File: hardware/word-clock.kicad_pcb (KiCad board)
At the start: 2 copper layers, 177.8 x 177.8 mm, 54 parts, among them SW1 Minute, SW2 Audio, SW3 Hour, U1 ESP32 CP2102, U2 74HC245

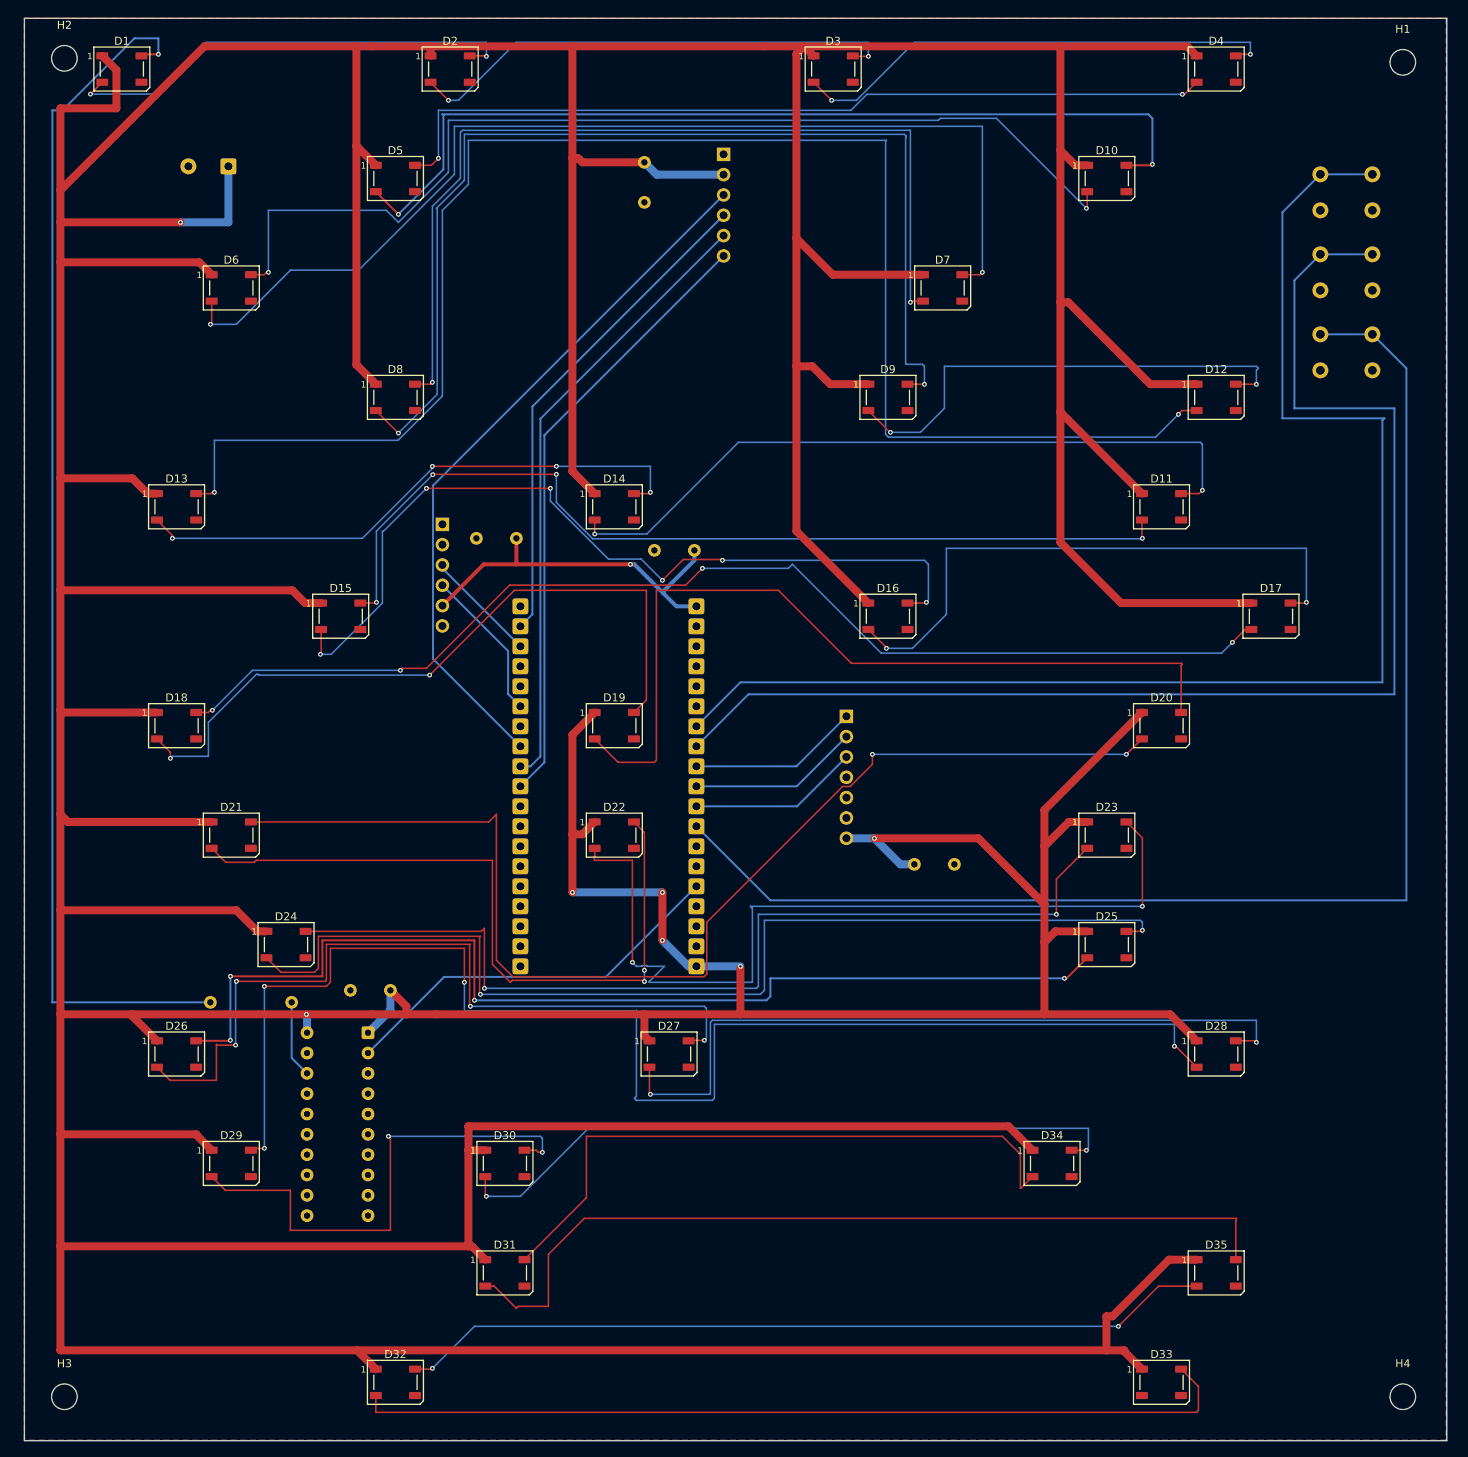
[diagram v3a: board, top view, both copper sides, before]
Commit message: feat(hardware): commit as-fabricated 63-LED board
The 63-LED board ordered from JLCPCB 2026-06-07 lived only in the working
tree and an untracked fab zip; the last hardware commit was the
superseded 35-LED April design. Commit the canonical KiCad source, the
custom daughtercard footprints (word-clock.pretty/ + fp-lib-table), and
the exact as-ordered fab package so the design that became the physical
clocks is under version control for the 40-year horizon.

Also add the pre-fab review and caliper-measured daughtercard dimensions,
and record the B.Cu +5V / F.Cu GND power-plane split in CLAUDE.md.
hardware/fab/README.md notes the WS2812B-B/W -> WS2812B-V6 (C52917433)
as-built LED substitution so the archived BOM is not misleading.
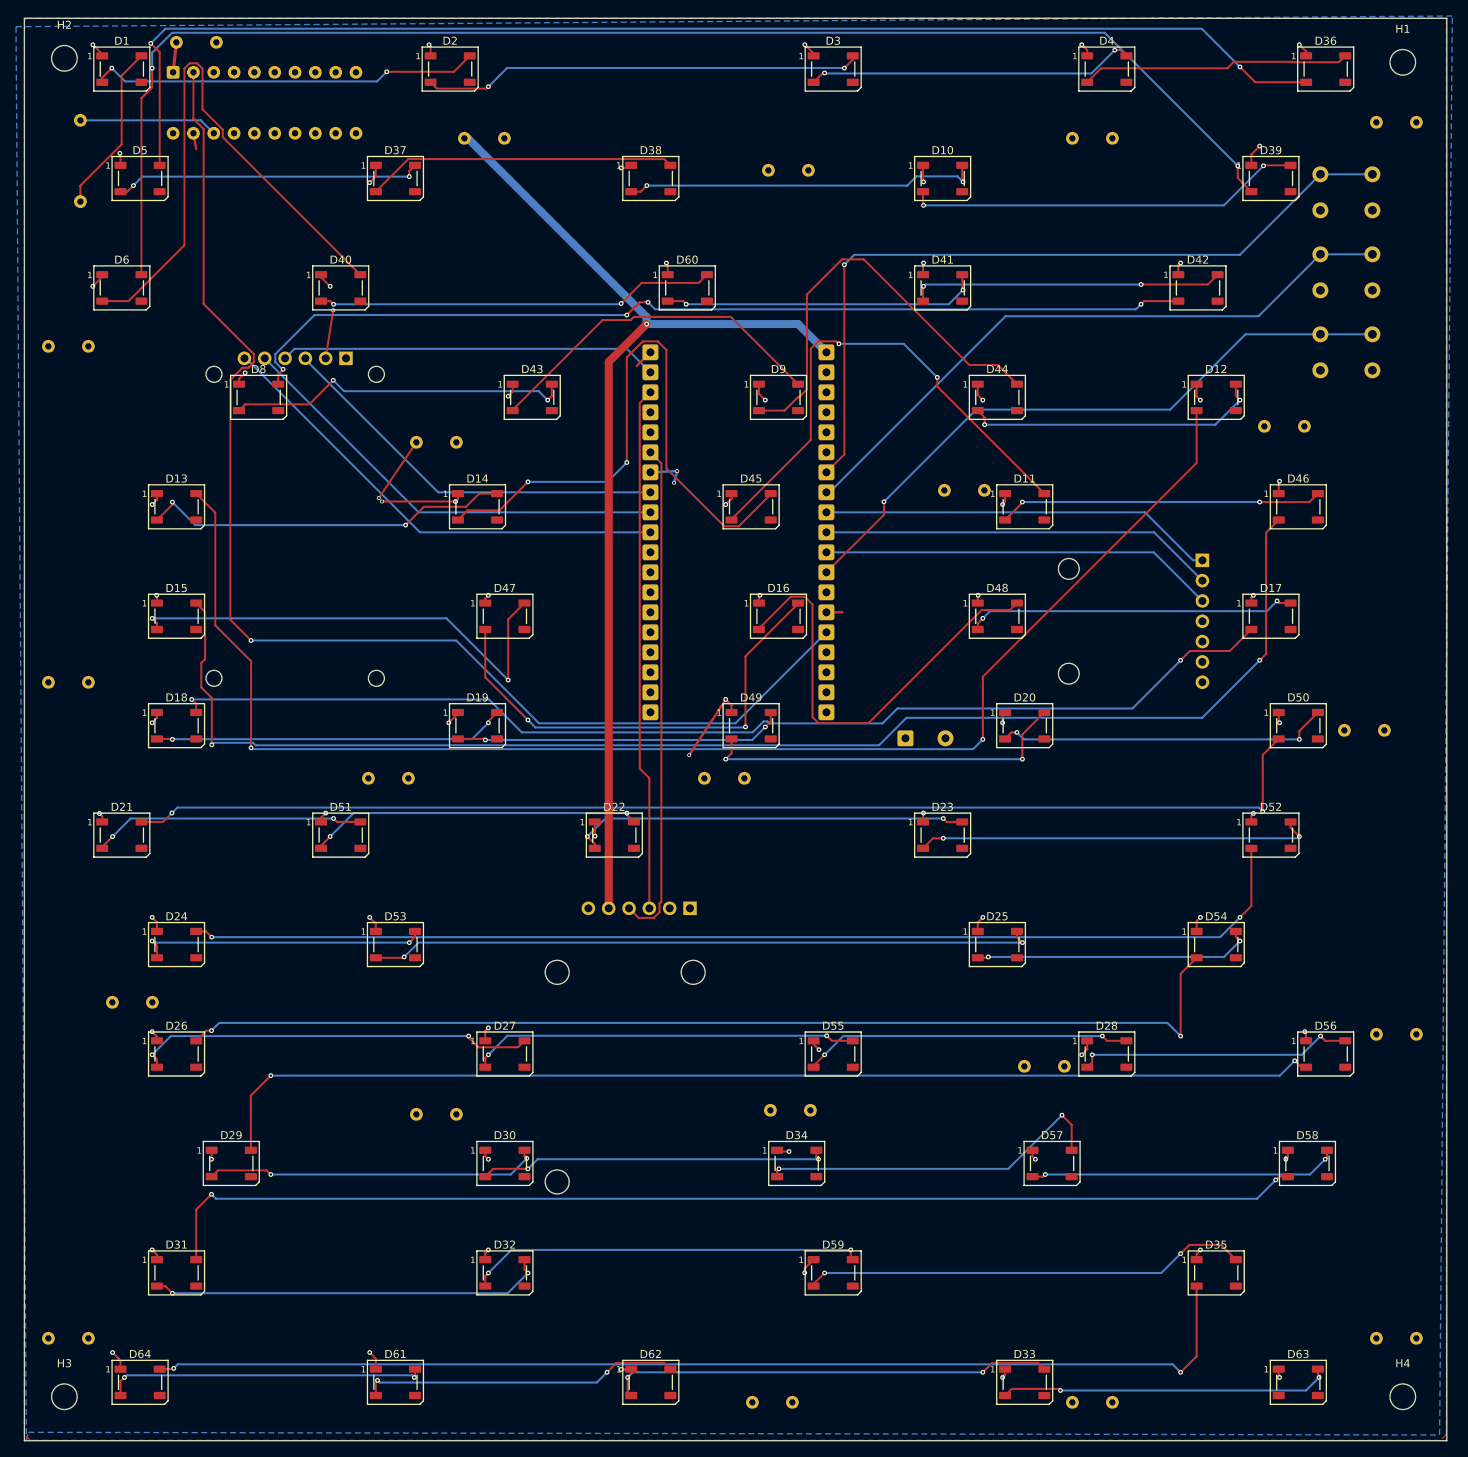
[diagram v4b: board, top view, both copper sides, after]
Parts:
- removed D7: LED_MINUTES, LED_SMD:LED_WS2812B_PLCC4_5.0x5.0mm_P3.2mm
- added C10: 100nF, Capacitor_THT:C_Disc_D5.0mm_W2.5mm_P5.00mm, B.Cu at (115.0, 59.0)
- added C11: 100nF, Capacitor_THT:C_Disc_D5.0mm_W2.5mm_P5.00mm, B.Cu at (3.00, 83.0)
- added C12: 100nF, Capacitor_THT:C_Disc_D5.0mm_W2.5mm_P5.00mm, B.Cu at (165.0, 89.0)
- added C13: 100nF, Capacitor_THT:C_Disc_D5.0mm_W2.5mm_P5.00mm, B.Cu at (43.0, 95.0)
- added C14: 100nF, Capacitor_THT:C_Disc_D5.0mm_W2.5mm_P5.00mm, B.Cu at (85.0, 95.0)
- added C15: 100nF, Capacitor_THT:C_Disc_D5.0mm_W2.5mm_P5.00mm, B.Cu at (11.0, 123.0)
- added C16: 100nF, Capacitor_THT:C_Disc_D5.0mm_W2.5mm_P5.00mm, B.Cu at (169.0, 127.0)
- added C17: 100nF, Capacitor_THT:C_Disc_D5.0mm_W2.5mm_P5.00mm, B.Cu at (125.0, 131.0)
- added C18: 100nF, Capacitor_THT:C_Disc_D5.0mm_W2.5mm_P5.00mm, B.Cu at (93.2, 136.5)
- added C19: 100nF, Capacitor_THT:C_Disc_D5.0mm_W2.5mm_P5.00mm, B.Cu at (49.0, 137.0)
- added C20: 100nF, Capacitor_THT:C_Disc_D5.0mm_W2.5mm_P5.00mm, B.Cu at (3.00, 165.0)
- added C21: 100nF, Capacitor_THT:C_Disc_D5.0mm_W2.5mm_P5.00mm, B.Cu at (169.0, 165.0)
- added C22: 100nF, Capacitor_THT:C_Disc_D5.0mm_W2.5mm_P5.00mm, B.Cu at (91.0, 173.0)
- added C23: 100nF, Capacitor_THT:C_Disc_D5.0mm_W2.5mm_P5.00mm, B.Cu at (131.0, 173.0)
- added C7: 100nF, Capacitor_THT:C_Disc_D5.0mm_W2.5mm_P5.00mm, B.Cu at (3.00, 41.0)
- added C8: 100nF, Capacitor_THT:C_Disc_D5.0mm_W2.5mm_P5.00mm, B.Cu at (155.0, 51.0)
- added C9: 100nF, Capacitor_THT:C_Disc_D5.0mm_W2.5mm_P5.00mm, B.Cu at (49.0, 53.0)
- added D36: LED_HALF_1, LED_SMD:LED_WS2812B_PLCC4_5.0x5.0mm_P3.2mm, F.Cu at (162.7, 6.34)
- added D37: LED_QUARTER_1, LED_SMD:LED_WS2812B_PLCC4_5.0x5.0mm_P3.2mm, F.Cu at (46.4, 20.0)
- added D38: LED_QUARTER_2, LED_SMD:LED_WS2812B_PLCC4_5.0x5.0mm_P3.2mm, F.Cu at (78.3, 20.0)
- added D39: LED_TWENTY_1, LED_SMD:LED_WS2812B_PLCC4_5.0x5.0mm_P3.2mm, F.Cu at (155.8, 20.0)
- added D40: LED_FIVE_MIN_1, LED_SMD:LED_WS2812B_PLCC4_5.0x5.0mm_P3.2mm, F.Cu at (39.5, 33.7)
- added D41: LED_MINUTES_1, LED_SMD:LED_WS2812B_PLCC4_5.0x5.0mm_P3.2mm, F.Cu at (114.8, 33.7)
- added D42: LED_MINUTES_2, LED_SMD:LED_WS2812B_PLCC4_5.0x5.0mm_P3.2mm, F.Cu at (146.7, 33.7)
- added D43: LED_HAPPY_1, LED_SMD:LED_WS2812B_PLCC4_5.0x5.0mm_P3.2mm, F.Cu at (63.5, 47.4)
- added D44: LED_PAST_1, LED_SMD:LED_WS2812B_PLCC4_5.0x5.0mm_P3.2mm, F.Cu at (121.6, 47.4)
- added D45: LED_BIRTH_1, LED_SMD:LED_WS2812B_PLCC4_5.0x5.0mm_P3.2mm, F.Cu at (90.8, 61.1)
- added D46: LED_THREE_1, LED_SMD:LED_WS2812B_PLCC4_5.0x5.0mm_P3.2mm, F.Cu at (159.2, 61.1)
- added D47: LED_ELEVEN_1, LED_SMD:LED_WS2812B_PLCC4_5.0x5.0mm_P3.2mm, F.Cu at (60.1, 74.7)
- added D48: LED_FOUR_1, LED_SMD:LED_WS2812B_PLCC4_5.0x5.0mm_P3.2mm, F.Cu at (121.6, 74.7)
- added D49: LED_EIGHT_1, LED_SMD:LED_WS2812B_PLCC4_5.0x5.0mm_P3.2mm, F.Cu at (90.8, 88.4)
- added D50: LED_SEVEN_1, LED_SMD:LED_WS2812B_PLCC4_5.0x5.0mm_P3.2mm, F.Cu at (159.2, 88.4)
- added D51: LED_NINE_1, LED_SMD:LED_WS2812B_PLCC4_5.0x5.0mm_P3.2mm, F.Cu at (39.5, 102.1)
- added D52: LED_TWELVE_1, LED_SMD:LED_WS2812B_PLCC4_5.0x5.0mm_P3.2mm, F.Cu at (155.8, 102.1)
- added D53: LED_NAME_1, LED_SMD:LED_WS2812B_PLCC4_5.0x5.0mm_P3.2mm, F.Cu at (46.4, 115.8)
- added D54: LED_FIVE_HR_1, LED_SMD:LED_WS2812B_PLCC4_5.0x5.0mm_P3.2mm, F.Cu at (149.0, 115.8)
- added D55: LED_OCLOCK_1, LED_SMD:LED_WS2812B_PLCC4_5.0x5.0mm_P3.2mm, F.Cu at (101.1, 129.5)
- added D56: LED_NOON_1, LED_SMD:LED_WS2812B_PLCC4_5.0x5.0mm_P3.2mm, F.Cu at (162.7, 129.5)
- added D57: LED_MORNING_1, LED_SMD:LED_WS2812B_PLCC4_5.0x5.0mm_P3.2mm, F.Cu at (128.5, 143.1)
- added D58: LED_MORNING_2, LED_SMD:LED_WS2812B_PLCC4_5.0x5.0mm_P3.2mm, F.Cu at (160.4, 143.1)
- added D59: LED_AFTERNOON_2, LED_SMD:LED_WS2812B_PLCC4_5.0x5.0mm_P3.2mm, F.Cu at (101.1, 156.8)
- added D60: LED_MINUTES, LED_SMD:LED_WS2812B_PLCC4_5.0x5.0mm_P3.2mm, F.Cu at (82.9, 33.7)
- added D61: LED_EVENING_1, LED_SMD:LED_WS2812B_PLCC4_5.0x5.0mm_P3.2mm, F.Cu at (46.4, 170.5)
- added D62: LED_EVENING_2, LED_SMD:LED_WS2812B_PLCC4_5.0x5.0mm_P3.2mm, F.Cu at (78.3, 170.5)
- added D63: LED_NIGHT_1, LED_SMD:LED_WS2812B_PLCC4_5.0x5.0mm_P3.2mm, F.Cu at (159.2, 170.5)
- added D64: LED_EVENING, LED_SMD:LED_WS2812B_PLCC4_5.0x5.0mm_P3.2mm, F.Cu at (14.5, 170.5)
- D32: value LED_EVENING -> LED_AFTERNOON_1
- J_AMP1: footprint Connector_PinHeader_2.54mm:PinHeader_1x07_P2.54mm_Vertical -> word-clock:Daughtercard_AMP_MAX98357A
- J_RTC1: footprint Connector_PinSocket_2.54mm:PinSocket_1x06_P2.54mm_Horizontal -> word-clock:Daughtercard_RTC_DS3231
- J_SD1: footprint Connector_PinSocket_2.54mm:PinSocket_1x06_P2.54mm_Horizontal -> word-clock:Daughtercard_SD_HW125
- U2: value 74HC245 -> 74HCT245
- moved U2 122.5 mm to (18.6, 6.75), turned to -90 degrees
- moved R1 113.4 mm to (7.00, 12.8), turned to -90 degrees
- moved C6 112.9 mm to (93.0, 19.0), turned to 0 degrees
- moved C2 110.8 mm to (110.1, 90.0), turned to 0 degrees
- moved C3 106.7 mm to (169.0, 13.0), turned to 0 degrees
- moved C1 90.7 mm to (19.0, 3.00), turned to 0 degrees
- moved J_RTC1 57.1 mm to (83.2, 111.2), turned to 90 degrees
- moved C5 54.1 mm to (131.0, 15.0), turned to 0 degrees
- moved J_SD1 53.6 mm to (40.2, 42.5), turned to 90 degrees
- moved C4 50.4 mm to (55.0, 15.0), turned to 0 degrees
- moved J_AMP1 48.6 mm to (147.2, 67.8)
- moved D31 41.0 mm to (19.0, 156.8)
- moved U1 35.7 mm to (89.2, 40.8)
- moved D34 31.9 mm to (96.5, 143.1)
- moved D5 31.9 mm to (14.5, 20.0)
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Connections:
- C1 pad 1: +3V3 -> +5V
- D14 pad 2: Net-(D11-DIN) -> Net-(D14-DOUT)
- D15 pad 4: Net-(D11-DOUT) -> Net-(D15-DIN)
- D16 pad 4: Net-(D15-DOUT) -> Net-(D16-DIN)
- D17 pad 4: Net-(D16-DOUT) -> Net-(D17-DIN)
- D20 pad 4: Net-(D19-DOUT) -> Net-(D20-DIN)
- D21 pad 4: Net-(D20-DOUT) -> Net-(D21-DIN)
- D22 pad 4: Net-(D21-DOUT) -> Net-(D22-DIN)
- D24 pad 4: Net-(D23-DOUT) -> Net-(D24-DIN)
- D25 pad 4: Net-(D24-DOUT) -> Net-(D25-DIN)
- D26 pad 4: Net-(D25-DOUT) -> Net-(D26-DIN)
- D28 pad 4: Net-(D27-DOUT) -> Net-(D28-DIN)
- D29 pad 4: Net-(D28-DOUT) -> Net-(D29-DIN)
- D32 pad 4: Net-(D32-DIN) -> Net-(D31-DOUT)
- D33 pad 2: unconnected-(D33-DOUT-Pad2) -> Net-(D33-DOUT)
- D33 pad 4: Net-(D32-DOUT) -> Net-(D33-DIN)
- D34 pad 2: Net-(D31-DIN) -> Net-(D34-DOUT)
- D35 pad 2: Net-(D32-DIN) -> Net-(D35-DOUT)
- D35 pad 4: Net-(D31-DOUT) -> Net-(D35-DIN)
- D4 pad 2: Net-(D4-DOUT) -> Net-(D36-DIN)
- D5 pad 2: Net-(D10-DIN) -> Net-(D37-DIN)
- D5 pad 4: Net-(D4-DOUT) -> Net-(D36-DOUT)
- D6 pad 4: Net-(D10-DOUT) -> Net-(D39-DOUT)
- D8 pad 2: Net-(D8-DOUT) -> Net-(D43-DIN)
- D9 pad 2: Net-(D12-DIN) -> Net-(D44-DIN)
- D9 pad 4: Net-(D8-DOUT) -> Net-(D43-DOUT)
- J_RTC1 pad 1: unconnected-(J_RTC1-32K-Pad1) -> GND
- J_RTC1 pad 2: unconnected-(J_RTC1-SQW-Pad2) -> +3V3
- J_RTC1 pad 3: /I2C_SCL -> /I2C_SDA
- J_RTC1 pad 4: /I2C_SDA -> /I2C_SCL
- J_RTC1 pad 5: +3V3 -> unconnected-(J_RTC1-SQW-Pad2)
- J_RTC1 pad 6: GND -> unconnected-(J_RTC1-32K-Pad1)
- J_SD1 pad 1: GND -> /SD_CS
- J_SD1 pad 2: +5V -> /SD_SCK
- J_SD1 pad 3: /SD_MISO -> /SD_MOSI
- J_SD1 pad 4: /SD_MOSI -> /SD_MISO
- J_SD1 pad 5: /SD_SCK -> +5V
- J_SD1 pad 6: /SD_CS -> GND
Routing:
- net +5V: track 1463.8 -> 137.9 mm, vias 7 -> 67
- net Net-(D39-DOUT): track 0.00 -> 175.9 mm, vias 0 -> 2
- net Net-(D15-DIN): track 0.00 -> 173.1 mm, vias 0 -> 2
- net Net-(D36-DOUT): track 0.00 -> 163.6 mm, vias 0 -> 2
- net Net-(D21-DIN): track 0.00 -> 151.0 mm, vias 0 -> 2
- net Net-(D24-DIN): track 0.00 -> 141.0 mm, vias 0 -> 2
- net Net-(D29-DIN): track 0.00 -> 140.9 mm, vias 0 -> 2
- net Net-(D28-DOUT): track 175.5 -> 34.7 mm, vias 4 -> 2
- net Net-(D35-DOUT): track 0.00 -> 139.9 mm, vias 0 -> 2
- net Net-(D8-DOUT): track 135.5 -> 0.00 mm, vias 2 -> 0
- net Net-(D26-DIN): track 0.00 -> 135.3 mm, vias 0 -> 2
- net /LED_DATA_OUT: track 152.4 -> 21.4 mm, vias 1 -> 0
- net /LED_DATA_3V3: track 49.7 -> 157.8 mm, vias 0 -> 1
- net Net-(D20-DOUT): track 147.7 -> 41.8 mm
- net Net-(D4-DOUT): track 105.5 -> 0.00 mm, vias 2 -> 0
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- added copper zone on B.Cu, net +5V
- removed copper zone on B.Cu, net GND
